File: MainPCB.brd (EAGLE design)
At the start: 139.7 x 114.3 mm, 79 parts, among them J2 DCJ0202, J3 FEMALE 2x3, X1 8MHz

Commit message: she done
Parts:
- added H10: STAND-OFF, SparkFun-Hardware:STAND-OFF
- moved H2 29.8 mm to (5.99, 77.2)
- moved H1 23.0 mm to (36.0, 84.0)
- moved H5 3.69 mm to (5.99, 107.4)
- moved H9 2.34 mm to (135.6, 110.5)
- moved H3 0.56 mm to (4.09, 4.09)
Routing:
- net SS: track 89.9 -> 87.3 mm
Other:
- board text added: "PA11"
- board text added: "PA12"
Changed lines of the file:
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@@
 <drawing>
 <settings>
-<setting alwaysvectorfont="yes"/>
+<setting alwaysvectorfont="no"/>
 <setting verticaltext="up"/>
 </settings>
@@
 Cynthia Zatlokowicz
 Mechor De La Garza</text>
+<text x="108.839" y="102.9208" size="1.27" layer="21">PA12</text>
+<text x="108.8136" y="94.5134" size="1.27" layer="21">PA11</text>
 </plain>
 <attributes>
@@
 <attribute name="VALUE" x="54.6154" y="36.6458" size="0.762" layer="28" font="vector" ratio="10" rot="MR180" align="top-left"/>
 </element>
-<element name="H1" library="SparkFun-Hardware" library_urn="urn:adsk.eagle:library:519" package="STAND-OFF" package3d_urn="urn:adsk.eagle:package:38630/1" value="STAND-OFF" x="35.2044" y="106.9614" rot="R90">
-<attribute name="NAME" x="33.1724" y="106.9614" size="0.762" layer="25" font="vector" ratio="10" rot="R90" align="bottom-center"/>
-<attribute name="VALUE" x="37.2364" y="106.9614" size="0.762" layer="27" font="vector" ratio="10" rot="R90" align="top-center"/>
-</element>
-<element name="H2" library="SparkFun-Hardware" library_urn="urn:adsk.eagle:library:519" package="STAND-OFF" package3d_urn="urn:adsk.eagle:package:38630/1" value="STAND-OFF" x="35.7952" y="77.5076" rot="R90">
-<attribute name="NAME" x="33.7632" y="77.5076" size="0.762" layer="25" font="vector" ratio="10" rot="R90" align="bottom-center"/>
-<attribute name="VALUE" x="37.8272" y="77.5076" size="0.762" layer="27" font="vector" ratio="10" rot="R90" align="top-center"/>
-</element>
-<element name="H3" library="SparkFun-Hardware" library_urn="urn:adsk.eagle:library:519" package="STAND-OFF" package3d_urn="urn:adsk.eagle:package:38630/1" value="STAND-OFF" x="4.5212" y="3.7338">
-<attribute name="NAME" x="4.5212" y="5.7658" size="0.762" layer="25" font="vector" ratio="10" align="bottom-center"/>
-<attribute name="VALUE" x="4.5212" y="1.7018" size="0.762" layer="27" font="vector" ratio="10" align="top-center"/>
+<element name="H1" library="SparkFun-Hardware" library_urn="urn:adsk.eagle:library:519" package="STAND-OFF" package3d_urn="urn:adsk.eagle:package:38630/1" value="STAND-OFF" x="36" y="84" rot="R90">
+<attribute name="NAME" x="33.968" y="84" size="0.762" layer="25" font="vector" ratio="10" rot="R90" align="bottom-center"/>
+<attribute name="VALUE" x="38.032" y="84" size="0.762" layer="27" font="vector" ratio="10" rot="R90" align="top-center"/>
+</element>
+<element name="H2" library="SparkFun-Hardware" library_urn="urn:adsk.eagle:library:519" package="STAND-OFF" package3d_urn="urn:adsk.eagle:package:38630/1" value="STAND-OFF" x="5.9944" y="77.216" rot="R90">
+<attribute name="NAME" x="3.9624" y="77.216" size="0.762" layer="25" font="vector" ratio="10" rot="R90" align="bottom-center"/>
+<attribute name="VALUE" x="8.0264" y="77.216" size="0.762" layer="27" font="vector" ratio="10" rot="R90" align="top-center"/>
+</element>
+<element name="H3" library="SparkFun-Hardware" library_urn="urn:adsk.eagle:library:519" package="STAND-OFF" package3d_urn="urn:adsk.eagle:package:38630/1" value="STAND-OFF" x="4.0894" y="4.0894">
+<attribute name="NAME" x="4.0894" y="6.1214" size="0.762" layer="25" font="vector" ratio="10" align="bottom-center"/>
+<attribute name="VALUE" x="4.0894" y="2.0574" size="0.762" layer="27" font="vector" ratio="10" align="top-center"/>
 </element>
 <element name="H4" library="SparkFun-Hardware" library_urn="urn:adsk.eagle:library:519" package="STAND-OFF" package3d_urn="urn:adsk.eagle:package:38630/1" value="STAND-OFF" x="38.7444" y="65.0508">
@@
 <attribute name="VALUE" x="66.4464" y="92.964" size="0.762" layer="27" font="vector" ratio="10" rot="R180" align="top-center"/>
 </element>
-<element name="H5" library="SparkFun-Hardware" library_urn="urn:adsk.eagle:library:519" package="STAND-OFF" package3d_urn="urn:adsk.eagle:package:38630/1" value="STAND-OFF" x="4.2206" y="110.6778">
-<attribute name="NAME" x="4.2206" y="112.7098" size="0.762" layer="25" font="vector" ratio="10" align="bottom-center"/>
-<attribute name="VALUE" x="4.2206" y="108.6458" size="0.762" layer="27" font="vector" ratio="10" align="top-center"/>
+<element name="H5" library="SparkFun-Hardware" library_urn="urn:adsk.eagle:library:519" package="STAND-OFF" package3d_urn="urn:adsk.eagle:package:38630/1" value="STAND-OFF" x="5.9944" y="107.442">
+<attribute name="NAME" x="5.9944" y="109.474" size="0.762" layer="25" font="vector" ratio="10" align="bottom-center"/>
+<attribute name="VALUE" x="5.9944" y="105.41" size="0.762" layer="27" font="vector" ratio="10" align="top-center"/>
 </element>
 <element name="H6" library="SparkFun-Hardware" library_urn="urn:adsk.eagle:library:519" package="STAND-OFF" package3d_urn="urn:adsk.eagle:package:38630/1" value="STAND-OFF" x="131.6978" y="10.1276">
@@
 <attribute name="VALUE" x="95.5662" y="71.7844" size="0.762" layer="27" font="vector" ratio="10" rot="R90"/>
 </element>
-<element name="H9" library="SparkFun-Hardware" library_urn="urn:adsk.eagle:library:519" package="STAND-OFF" package3d_urn="urn:adsk.eagle:package:38630/1" value="STAND-OFF" x="133.2484" y="110.4646">
-<attribute name="NAME" x="133.2484" y="112.4966" size="0.762" layer="25" font="vector" ratio="10" align="bottom-center"/>
-<attribute name="VALUE" x="133.2484" y="108.4326" size="0.762" layer="27" font="vector" ratio="10" align="top-center"/>
+<element name="H9" library="SparkFun-Hardware" library_urn="urn:adsk.eagle:library:519" package="STAND-OFF" package3d_urn="urn:adsk.eagle:package:38630/1" value="STAND-OFF" x="135.5852" y="110.49">
+<attribute name="NAME" x="135.5852" y="112.522" size="0.762" layer="25" font="vector" ratio="10" align="bottom-center"/>
+<attribute name="VALUE" x="135.5852" y="108.458" size="0.762" layer="27" font="vector" ratio="10" align="top-center"/>
 </element>
 <element name="R12" library="SparkFun-Resistors" library_urn="urn:adsk.eagle:library:532" package="0603" package3d_urn="urn:adsk.eagle:package:39650/1" value="100k" x="69.317" y="104.3254" rot="R270">
@@
 <attribute name="PROD_ID" value="RES-07828" x="131.8006" y="75.2602" size="1.778" layer="27" rot="R90" display="off"/>
 <attribute name="VALUE" x="132.5626" y="75.2602" size="0.6096" layer="27" font="vector" ratio="20" rot="R90" align="top-center"/>
+</element>
+<element name="H10" library="SparkFun-Hardware" library_urn="urn:adsk.eagle:library:519" package="STAND-OFF" package3d_urn="urn:adsk.eagle:package:38630/1" value="STAND-OFF" x="135.5852" y="4.0894">
+<attribute name="NAME" x="135.5852" y="6.1214" size="0.6096" layer="25" font="vector" ratio="20" align="bottom-center"/>
+<attribute name="VALUE" x="135.5852" y="2.0574" size="0.6096" layer="27" font="vector" ratio="20" align="top-center"/>
 </element>
 </elements>
@@
 <wire x1="78.10425625" y1="82.9818" x2="75.3364" y2="82.9818" width="0.1524" layer="1"/>
 <wire x1="74.9554" y1="82.6008" x2="70.2564" y2="87.2998" width="0.1524" layer="16"/>
-<wire x1="70.2564" y1="87.2998" x2="70.2564" y2="87.3252" width="0.1524" layer="16"/>
-<wire x1="70.2564" y1="87.3252" x2="57.3532" y2="87.3252" width="0.1524" layer="16"/>
-<wire x1="57.3532" y1="87.3252" x2="55.7022" y2="85.6742" width="0.1524" layer="16"/>
-<wire x1="55.7022" y1="85.6742" x2="33.9852" y2="85.6742" width="0.1524" layer="16"/>
-<wire x1="33.9852" y1="85.6742" x2="17.2974" y2="102.362" width="0.1524" layer="16"/>
-<wire x1="17.2974" y1="102.362" x2="17.353" y2="102.4176" width="0.1524" layer="16"/>
-<wire x1="17.353" y1="102.4176" x2="17.353" y2="105.9976" width="0.1524" layer="16"/>
+<wire x1="70.2564" y1="87.2998" x2="56.515" y2="87.2998" width="0.1524" layer="16"/>
+<wire x1="56.515" y1="87.2998" x2="55.372" y2="86.1568" width="0.1524" layer="16"/>
+<wire x1="55.372" y1="86.1568" x2="43.3578" y2="86.1568" width="0.1524" layer="16"/>
+<wire x1="43.3578" y1="86.1568" x2="26.3144" y2="103.2002" width="0.1524" layer="16"/>
+<wire x1="26.3144" y1="103.2002" x2="20.1504" y2="103.2002" width="0.1524" layer="16"/>
+<wire x1="20.1504" y1="103.2002" x2="17.353" y2="105.9976" width="0.1524" layer="16"/>
 </signal>
 <signal name="TX_ESP">

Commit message: major changes
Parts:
- removed C11, C24, C25, C26: 0.1uF, SparkFun-Capacitors:0603
- removed JP1: (no value), pinhead:2X06
- removed R17: 1k, SparkFun-Resistors:0603
- removed R18, R19: 100, SparkFun-Resistors:0603
- removed S2, S3: MOMENTARY-SWITCH-SPST-SMD-6.0X3.5MM, SparkFun-Switches:TACTILE_SWITCH_SMD_6.0X3.5MM
- removed U$7: ESP32, SeniorDesignParts:38-SMD
- added J4: (no value), SparkFun-Connectors:2X4
- added JP5: (no value), pinhead:1X08
- moved H1 50.9 mm to (1.00, 121.0)
- moved R10 49.5 mm to (112.8, 52.0)
- moved R13 49.5 mm to (86.9, 51.2)
- moved S1 49.5 mm to (76.0, 60.0)
- moved C13 49.5 mm to (73.4, 43.1)
- moved C5 49.5 mm to (95.1, 44.2)
- moved C6 49.5 mm to (90.2, 44.2)
- moved C7 49.5 mm to (90.4, 39.5)
- moved D1 49.5 mm to (117.6, 52.0)
- moved D2 49.5 mm to (117.6, 48.9)
- moved R11 49.5 mm to (112.7, 48.9)
- moved R12 49.5 mm to (76.3, 55.3)
- moved U$1 49.5 mm to (92.6, 41.8)
- moved C12 49.5 mm to (73.4, 47.9)
- moved C14 49.5 mm to (79.1, 55.4)
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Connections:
- removed net EN: C24.1, C26.1, R17.1, S2.2, U$7.3
- removed net IO0: C25.1, S3.2, U$7.25
- removed net N$10: R19.2, U$7.34
- removed net N$8: R18.2, U$7.35
- new net IRQ: JP5.4
- new net RST: JP5.2
- new net SCK: JP5.7
- new net SDA: JP5.8
- net 3.3V: now also JP5.1; no longer C11.1, JP1.1, R17.2, U$7.2
- net GND: now also JP5.3; no longer C11.2, C24.2, C25.2, C26.2, JP1.11, S2.1, S3.1, U$7.1, U$7.15, U$7.38, U$7.39
- net MISO: now also JP5.5; no longer JP1.5
- net MOSI: now also JP5.6; no longer JP1.2
- net RX_ESP: no longer R19.1
- net SCLK: no longer JP1.6
- net SS: no longer JP1.10
- net TX_ESP: no longer R18.1
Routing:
- net 3.3V: track 521.0 -> 276.0 mm
- net SCLK: track 98.7 -> 1.63 mm, vias 3 -> 1
- net MOSI: track 86.7 -> 3.85 mm, vias 2 -> 1
- net SS: track 87.3 -> 7.73 mm, vias 1 -> 0
- net COLOUT_2: track 88.6 -> 17.2 mm
- net ROWOUT_7: track 81.3 -> 10.9 mm
- net ROWOUT_1: track 83.3 -> 12.9 mm
- net ROWOUT_2: track 79.1 -> 14.9 mm
- net COLOUT_8: track 105.3 -> 41.4 mm
- net COLOUT_3: track 84.7 -> 20.8 mm
- net COLOUT_1: track 87.2 -> 23.6 mm
- net COLOUT_6: track 95.1 -> 32.1 mm
- net ROWOUT_4: track 80.8 -> 18.3 mm
- net COLOUT_4: track 90.9 -> 28.4 mm
- net MISO: track 66.3 -> 3.87 mm
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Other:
- board size 139.7 x 114.3 mm -> 139.7 x 76.2 mm

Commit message: lotta changes
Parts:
- moved H1 81.1 mm to (5.00, 40.0)
- moved H2 60.5 mm to (27.0, 69.2)
- moved H5 55.5 mm to (5.99, 69.4)
- moved J3 48.7 mm to (133.0, 45.0), turned to 270 degrees
- moved R16 43.7 mm to (127.8, 44.9)
- moved R14 43.6 mm to (127.6, 39.6)
- moved R15 43.4 mm to (127.7, 42.5)
- moved C2 38.7 mm to (26.2, 84.0)
- moved H9 38.5 mm to (134.8, 72.0)
- moved U$4 38.0 mm to (19.0, 92.1)
- moved C1 37.2 mm to (11.9, 83.4)
- moved C3 21.4 mm to (28.3, 35.8), turned to 180 degrees
- moved C14 17.9 mm to (90.7, 69.1), flipped to the bottom, turned to 90 degrees
- moved JP2 17.3 mm to (99.6, 72.4)
- moved R12 16.5 mm to (85.8, 68.8), flipped to the bottom, turned to 90 degrees
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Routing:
- net +5V: track 95.9 -> 5.04 mm, vias 1 -> 0
- net 3.3V: track 276.0 -> 219.8 mm
- net COL8: track 39.4 -> 9.90 mm
- net COL9: track 42.8 -> 13.5 mm
- net NRST: track 33.9 -> 5.34 mm, vias 2 -> 1
- net ROW2: track 52.5 -> 24.8 mm
- net ROW1: track 39.5 -> 14.7 mm
- net COL5: track 30.3 -> 7.83 mm
- net ROW8: track 28.6 -> 6.53 mm, vias 1 -> 0
- net COL6: track 33.3 -> 11.8 mm
- net COL7: track 37.2 -> 17.1 mm
- net SWDIO: track 22.4 -> 3.41 mm, vias 2 -> 1
- net COLOUT_7: track 41.9 -> 24.6 mm
- net COL2: track 22.0 -> 5.72 mm
- net COL1: track 19.0 -> 3.42 mm
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- added copper zone on layer 1, net 9V
- added copper zone on layer 1, net N$3

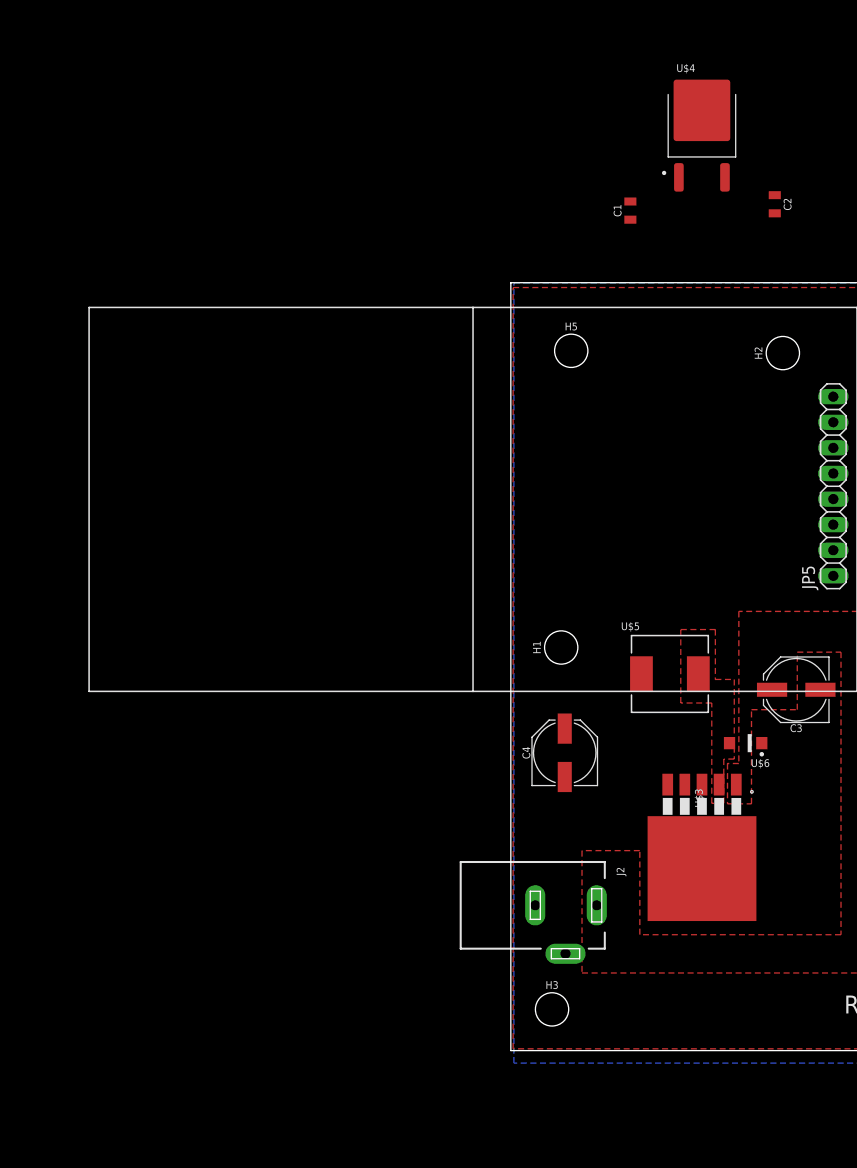
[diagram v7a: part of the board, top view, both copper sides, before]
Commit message: 3.3V reguator
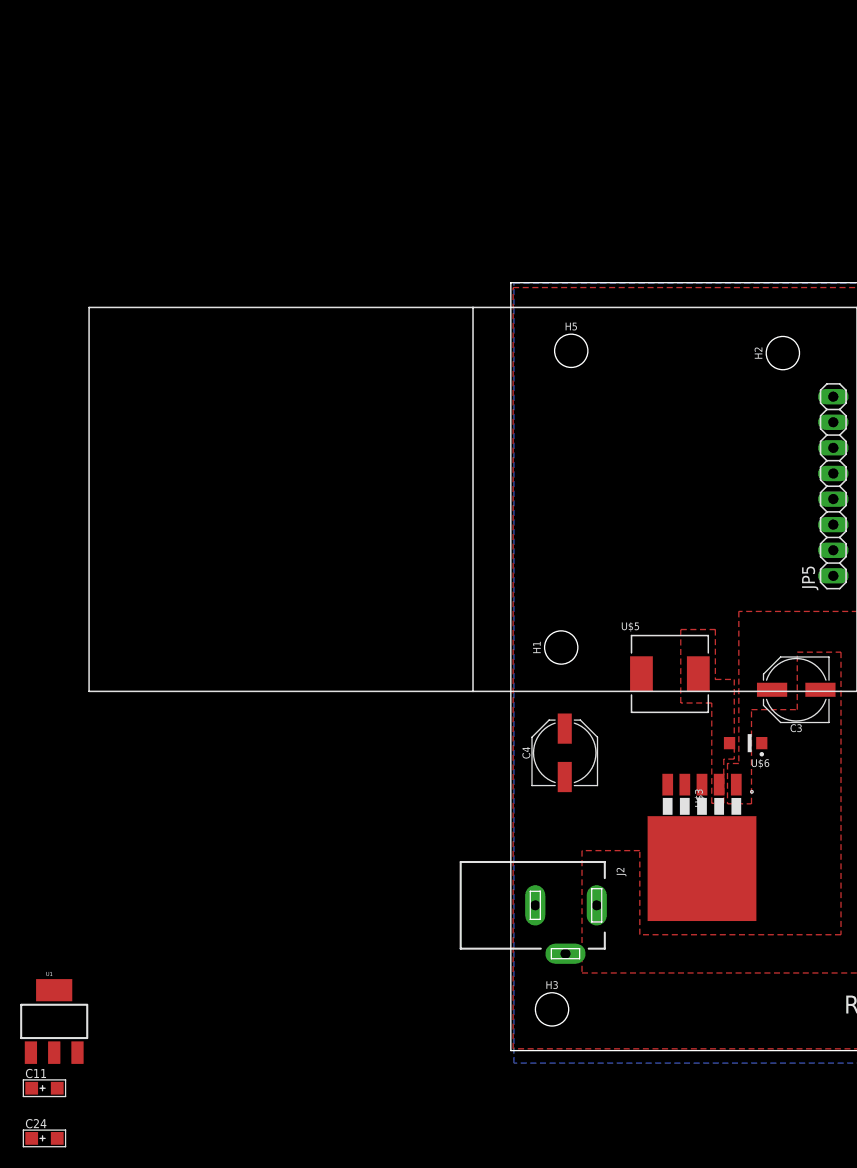
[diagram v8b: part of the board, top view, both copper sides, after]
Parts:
- removed C1, C2: 10uF, SparkFun-Capacitors:0805
- removed U$4: AP7363, SeniorDesignParts:T0-252
- added C11, C24: 10uf, Seeed-Capacitor:AVX-A
- added U1: (no value), SparkFun-IC-Power:SOT223
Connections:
- net +5V: now also C24.+, U1.3; no longer C1.1, U$4.1
- net 3.3V: now also C11.+, U1.2; no longer C2.1, U$4.3
- net GND: now also C11.-, C24.-, U1.1, U1.4; no longer C1.2, C2.2, U$4.2
